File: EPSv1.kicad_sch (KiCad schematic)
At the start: 0 parts

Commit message: first commit
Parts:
- added BT1, BT2: Battery_Cell, symbol Device:Battery_Cell
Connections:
- net BQ29700_1/CELL+: now also BT1.1 (+)
- net BQ29700_1/CELL-: now also BT1.2 (-)
- net BQ29700_2/CELL+: now also BT2.1 (+)
- net BQ29700_2/CELL-: now also BT2.2 (-)
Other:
- sheet Untitled Sheet renamed MCP73831_1
- added sheet MCP73831_2 (../PCB_Schematic_Blocks_Library/MCP73831.kicad_sch)
- sheet MCP73831_1 ports: added GND; removed none

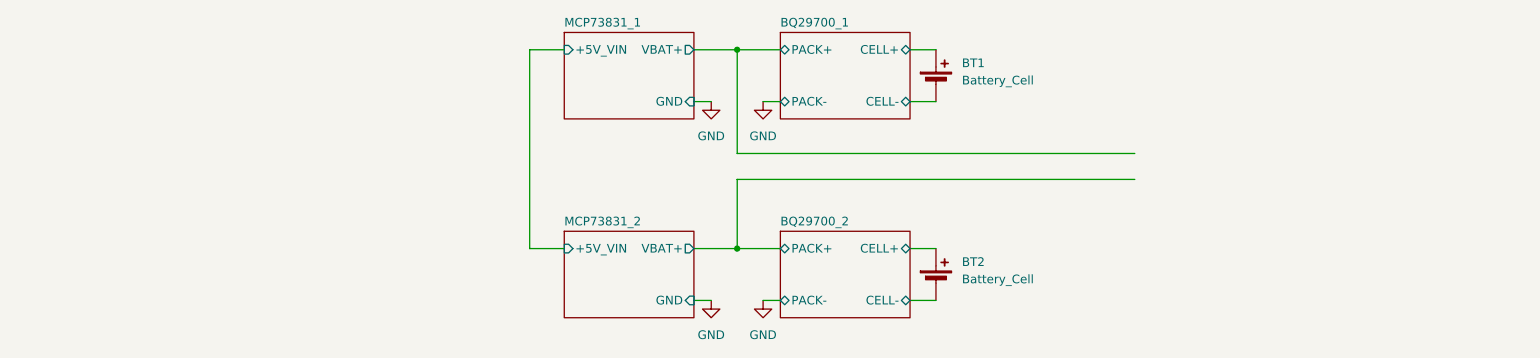
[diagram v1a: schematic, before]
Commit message: added molex nanofit
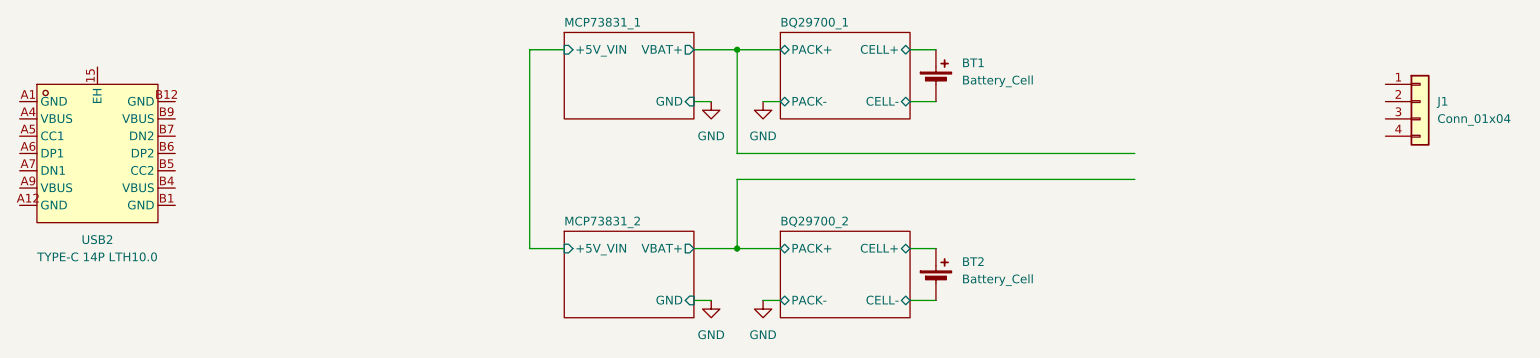
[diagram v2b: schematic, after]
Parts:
- added J1: Conn_01x04, Rocketry_Manual:1054301102, symbol Connector_Generic:Conn_01x04
- added USB2: TYPE-C 14P LTH10.0, Rocketry_Easyeda:TYPE-C-SMD_918-468K2029Y50001, symbol Rocketry_Easyeda:TYPE-C14PLTH10.0
- BT1, BT2: footprint (none) -> Rocketry_Manual:BAT_1121
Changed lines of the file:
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@@
 			)
 		)
-		(property "Footprint" ""
+		(property "Footprint" "Rocketry_Manual:BAT_1121"
 			(at 156.21 94.996 90)
 			(effects
@@
 				(path "/61d36b12-c329-4dd2-b08b-b63678fc7b25"
 					(reference "BT2")
+					(unit 1)
+				)
+			)
+		)
+	)
+	(symbol
+		(lib_id "Rocketry_Easyeda:TYPE-C14PLTH10.0")
+		(at 33.02 76.2 0)
+		(unit 1)
+		(exclude_from_sim no)
+		(in_bom yes)
+		(on_board yes)
+		(dnp no)
+		(fields_autoplaced yes)
+		(property "Reference" "USB2"
+			(at 33.02 90.17 0)
+			(effects
+				(font
+					(size 1.27 1.27)
+				)
+			)
+		)
+		(property "Value" "TYPE-C 14P LTH10.0"
+			(at 33.02 92.71 0)
+			(effects
+				(font
+					(size 1.27 1.27)
+				)
+			)
+		)
+		(property "Footprint" "Rocketry_Easyeda:TYPE-C-SMD_918-468K2029Y50001"
+			(at 33.02 92.71 0)
+			(effects
+				(font
+					(size 1.27 1.27)
+				)
+				(hide yes)
+			)
+		)
+		(property "Datasheet" ""
+			(at 33.02 76.2 0)
+			(effects
+				(font
+					(size 1.27 1.27)
+				)
+				(hide yes)
+			)
+		)
+		(property "Description" ""
+			(at 33.02 76.2 0)
+			(effects
+				(font
+					(size 1.27 1.27)
+				)
+				(hide yes)
+			)
+		)
+		(property "LCSC Part" "C5187467"
+			(at 33.02 95.25 0)
+			(effects
+				(font
+					(size 1.27 1.27)
+				)
+				(hide yes)
+			)
+		)
+		(pin "B9"
+		)
+		(pin "B4"
+		)
+		(pin "A9"
+		)
+		(pin "B7"
+		)
+		(pin "A4"
+		)
+		(pin "A12"
+		)
+		(pin "A1"
+		)
+		(pin "B5"
+		)
+		(pin "B12"
+		)
+		(pin "15"
+		)
+		(pin "A5"
+		)
+		(pin "A6"
+		)
+		(pin "B6"
+		)
+		(pin "A7"
+		)
+		(pin "B1"
+		)
+		(instances
+			(project ""
+				(path "/61d36b12-c329-4dd2-b08b-b63678fc7b25"
+					(reference "USB2")
+					(unit 1)
+				)
+			)
+		)
+	)
+	(symbol
+		(lib_id "Connector_Generic:Conn_01x04")
+		(at 227.33 69.85 0)
+		(unit 1)
+		(exclude_from_sim no)
+		(in_bom yes)
+		(on_board yes)
+		(dnp no)
+		(fields_autoplaced yes)
+		(property "Reference" "J1"
+			(at 229.87 69.8499 0)
+			(effects
+				(font
+					(size 1.27 1.27)
+				)
+				(justify left)
+			)
+		)
+		(property "Value" "Conn_01x04"
+			(at 229.87 72.3899 0)
+			(effects
+				(font
+					(size 1.27 1.27)
+				)
+				(justify left)
+			)
+		)
+		(property "Footprint" "Rocketry_Manual:1054301102"
+			(at 227.33 69.85 0)
+			(effects
+				(font
+					(size 1.27 1.27)
+				)
+				(hide yes)
+			)
+		)
+		(property "Datasheet" "~"
+			(at 227.33 69.85 0)
+			(effects
+				(font
+					(size 1.27 1.27)
+				)
+				(hide yes)
+			)
+		)
+		(property "Description" "Generic connector, single row, 01x04, script generated (kicad-library-utils/schlib/autogen/connector/)"
+			(at 227.33 69.85 0)
+			(effects
+				(font
+					(size 1.27 1.27)
+				)
+				(hide yes)
+			)
+		)
+		(pin "2"
+		)
+		(pin "3"
+		)
+		(pin "4"
+		)
+		(pin "1"
+		)
+		(instances
+			(project ""
+				(path "/61d36b12-c329-4dd2-b08b-b63678fc7b25"
+					(reference "J1")
 					(unit 1)
 				)
@@
 		(dnp no)
 		(fields_autoplaced yes)
-		(property "Reference" "#PWR01"
+		(property "Reference" "#PWR02"
 			(at 123.19 105.41 0)
 			(effects
@@
 			(project ""
 				(path "/61d36b12-c329-4dd2-b08b-b63678fc7b25"
-					(reference "#PWR01")
+					(reference "#PWR02")
 					(unit 1)
 				)
@@
 			)
 		)
-		(property "Footprint" ""
+		(property "Footprint" "Rocketry_Manual:BAT_1121"
 			(at 156.21 65.786 90)
 			(effects
@@
 		(dnp no)
 		(fields_autoplaced yes)
-		(property "Reference" "#PWR02"
+		(property "Reference" "#PWR01"
 			(at 123.19 76.2 0)
 			(effects
@@
 			(project "EPSv1"
 				(path "/61d36b12-c329-4dd2-b08b-b63678fc7b25"
-					(reference "#PWR02")
-					(unit 1)
-				)
+					(reference "#PWR01")
+					(unit 1)
+				)

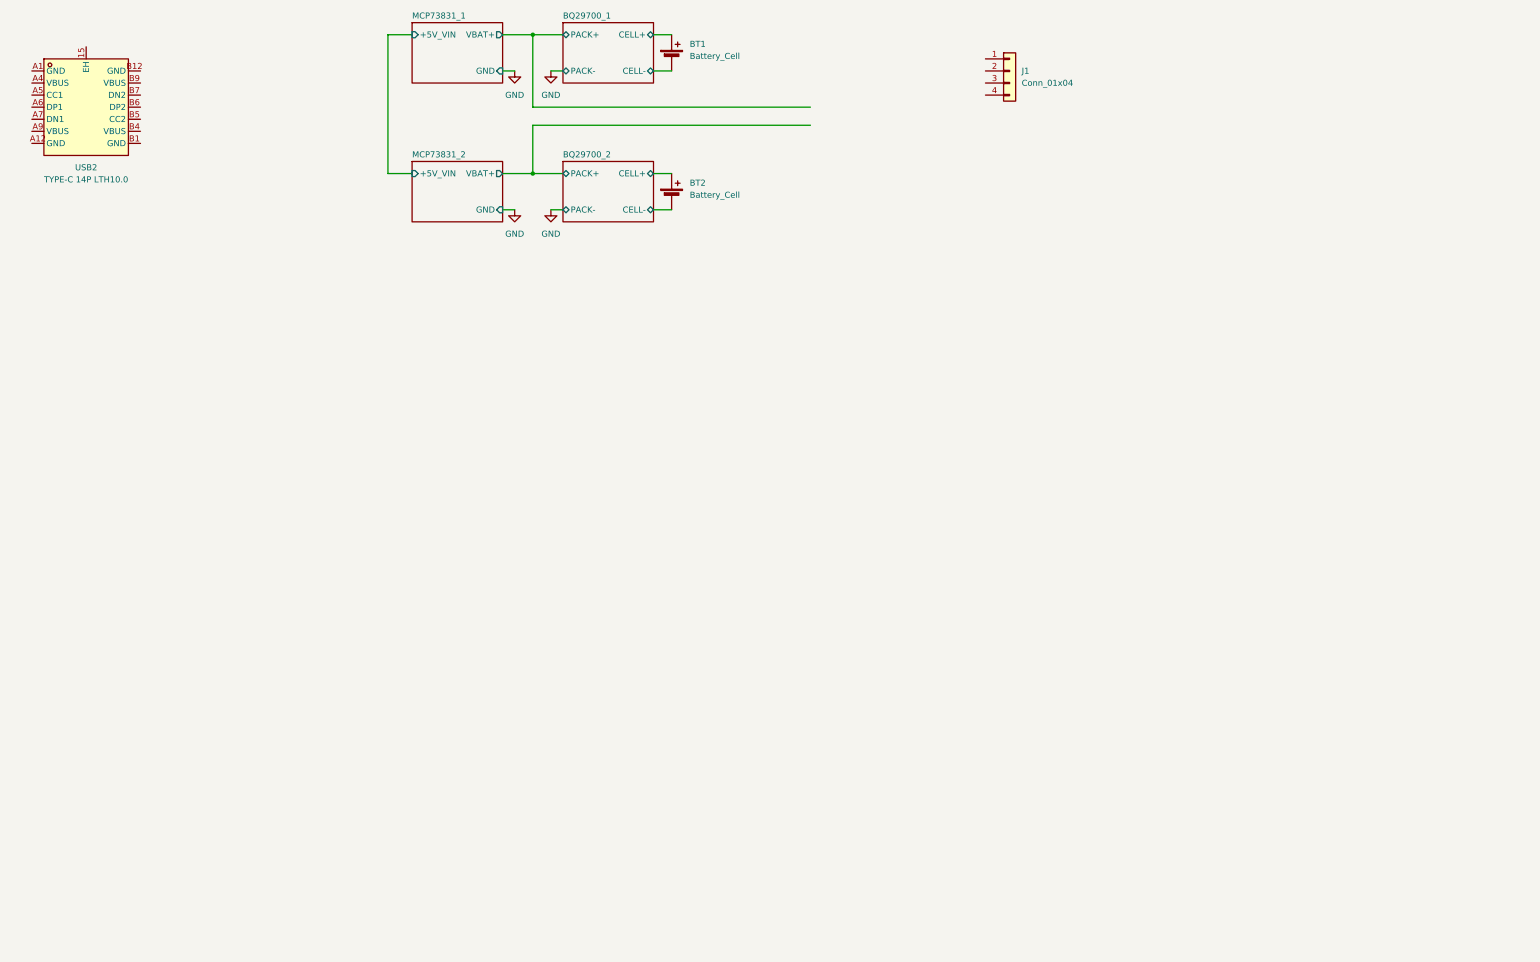
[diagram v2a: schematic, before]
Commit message: Laid out all the blocks and imported the board outline
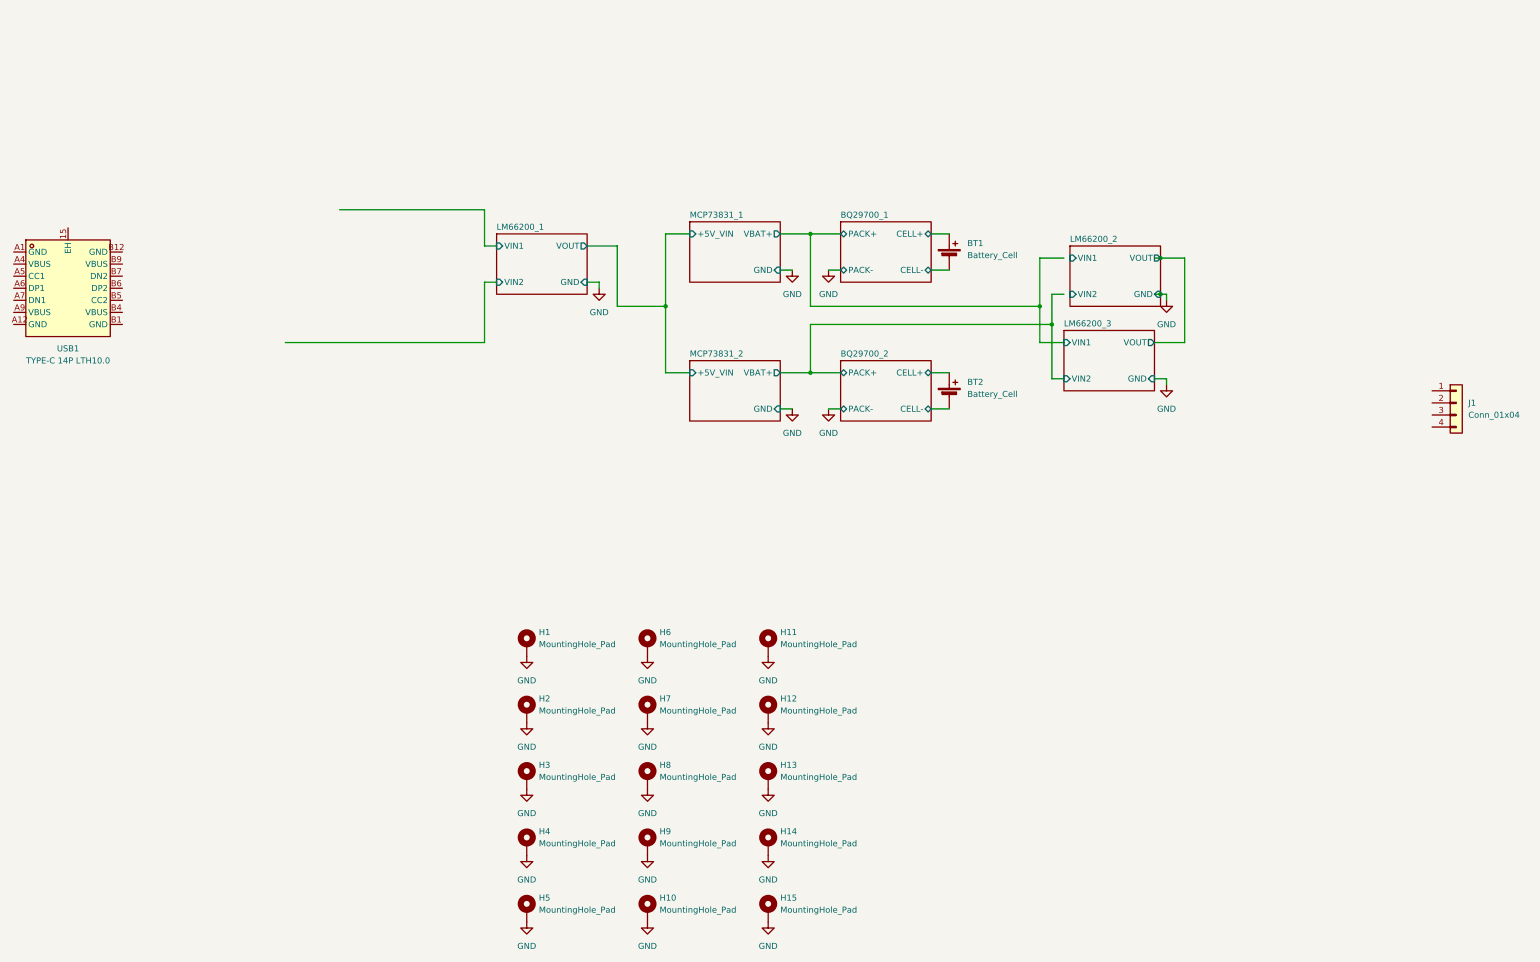
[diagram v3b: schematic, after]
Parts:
- added H1, H10, H11, H12, H13, H14, H15, H2, H3, H4, H5, H6, H7, H8, H9: MountingHole_Pad, MountingHole:MountingHole_2.7mm_M2.5_Pad_Via, symbol Mechanical:MountingHole_Pad
- renumbered USB2 to USB1
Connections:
- net GND: now also H1.1, H10.1, H11.1, H12.1, H13.1, H14.1, H15.1, H2.1, H3.1, H4.1, H5.1, H6.1, H7.1, H8.1, H9.1
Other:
- added sheet LM66200_1 (../PCB_Schematic_Blocks_Library/LM66200.kicad_sch)
- added sheet LM66200_2 (../PCB_Schematic_Blocks_Library/LM66200.kicad_sch)
- added sheet LM66200_3 (../PCB_Schematic_Blocks_Library/LM66200.kicad_sch)
- moved on the sheet: BT1, BT2, J1, USB1

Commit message: 100x100 board size
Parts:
- removed H10, H11, H12, H13, H14, H15, H5, H6, H7, H8, H9: MountingHole_Pad, MountingHole:MountingHole_2.7mm_M2.5_Pad_Via, symbol Mechanical:MountingHole_Pad
- added J3, J4: Molex_Microfit, Rocketry_Manual:1054301102, symbol Connector_Generic:Conn_01x04
- added U10: MCP9700AT-E/TT, Rocketry_Easyeda:SOT-23-3_L2.9-W1.3-P1.90-LS2.4-BR, symbol Rocketry_Easyeda:MCP9700AT-E_TT
- J1: value Conn_01x04 -> Molex_Microfit
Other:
- added sheet LM66200_4 (../PCB_Schematic_Blocks_Library/LM66200.kicad_sch)
- added sheet LM66200_5 (../PCB_Schematic_Blocks_Library/LM66200.kicad_sch)
- added sheet LM66200_6 (../PCB_Schematic_Blocks_Library/LM66200.kicad_sch)
- added sheet STM32L432KCUx (../PCB_Schematic_Blocks_Library/STM32L432KCUx.kicad_sch)
- sheet LM66200_1 ports: added ~{ON}; removed none
- sheet LM66200_2 ports: added ~{ON}; removed none
- sheet LM66200_3 ports: added ~{ON}; removed none
- moved on the sheet: BT1, BT2, H1, H2, H3, J1, USB1

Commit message: adde new blocks
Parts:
- added R1, R2, R3, R4: 470k 0603, Rocketry_Easyeda:R0603, symbol Rocketry_Easyeda:0603WAF4703T5E (470k 0603)
- added U1: MCP9700AT-E/TT, Rocketry_Easyeda:SOT-23-3_L2.9-W1.3-P1.90-LS2.4-BR, symbol Rocketry_Easyeda:MCP9700AT-E_TT
- renumbered J4 to J1, J3 to J2, J1 to J3, U10 to U2
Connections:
- net GND: now also U2.3 (GND), R2.1, R4.1, U1.3 (GND)
- net +5V: now reaches U2.1 (VDD)
- net +5V: now also U1.1 (VDD)
- net PB1: now reaches U2.2 (VOUT)
- net BQ29700_1/CELL+ renamed CELL_1+
- net CELL_1+: now also R1.2
- net BQ29700_2/CELL+ renamed CELL_2+
- net CELL_2+: now also R3.2
- new net PA0: R1.1, R2.2
- new net PA1: R3.1, R4.2
- new net PB0: U1.2 (VOUT)
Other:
- added sheet Reverse_Polarity (../PCB_Schematic_Blocks_Library/Reverse_Polarity_Block.kicad_sch)
- added sheet TPS63070_3.3V (../PCB_Schematic_Blocks_Library/TPS63070_3.3V.kicad_sch)
- moved on the sheet: H1, H2, H3, H4, U2

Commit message: exported STEP
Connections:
- net +3.3V: now also U1.1 (VDD), U2.1 (VDD)
- net +5V: no longer U1.1 (VDD), U2.1 (VDD)
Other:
- added sheet TPS63070_5V (../PCB_Schematic_Blocks_Library/TPS63070_5V.kicad_sch)
- moved on the sheet: BT1, BT2, U1, U2, USB1

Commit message: started proper layout
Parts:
- removed BT1, BT2: Battery_Cell, Rocketry_Manual:BAT_1121, symbol Device:Battery_Cell
- removed J1, J2, J3: Molex_Microfit, Rocketry_Manual:1054301102, symbol Connector_Generic:Conn_01x04
- removed USB1: TYPE-C 14P LTH10.0, Rocketry_Easyeda:TYPE-C-SMD_918-468K2029Y50001, symbol Rocketry_Easyeda:TYPE-C14PLTH10.0
- added BT1: 2P 21700 Cell Holder, Rocketry_Manual:PA21700x2-THM_Parallel, symbol Connector_Generic:Conn_02x02_Counter_Clockwise
- added J1, J3, J4: 1053091102, Rocketry_Manual:CON_1053091102, symbol Rocketry_Manual:1053091102
- added R36, R37, R38: 100k 0603, Rocketry_Easyeda:R0603, symbol Rocketry_Easyeda:0603WAF1003T5E (100k 0603)
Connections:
- net CELL_1+: now also BT1.4 (Pin_4)
- net CELL_2+: now also BT1.1 (Pin_1)
- net GND: now also J1.2, J3.2, J4.2, R36.1, R37.1, R38.1
- net LM66200_4/VOUT: now also J1.1
- net LM66200_5/VOUT: now also J3.1
- net LM66200_6/VOUT: now also J4.1
- net ~{MCU_LS_1}: now also R36.2
- net ~{MCU_LS_2}: now also R37.2
- net ~{MCU_LS_3}: now also R38.2
- new net CELL_1-: BT1.3 (Pin_3)
- new net CELL_2-: BT1.2 (Pin_2)
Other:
- sheet STM32L432KCUx ports: added USB_+5V; removed none
- note added: "100k pulldowns to keep the default state ON"

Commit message: v0.1 sent to JLCPCB
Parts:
- added C37, C38, C39, C40, C41, C42, C43, C44, C45, C46: 10uF 0603, Rocketry_Easyeda:C0603, symbol Rocketry_Easyeda:CL10A106KP8NNNC (10uF 0603)
- added TP1, TP10, TP2, TP3, TP4, TP5, TP6, TP7, TP8, TP9: TestPoint, TestPoint:TestPoint_Pad_1.0x1.0mm, symbol Connector:TestPoint
- added U26: 1.5uF 2.9A, Rocketry_Easyeda:IND-SMD_L2.5-W2.0_MEKK2520TR47M, symbol Rocketry_Easyeda:FTC252012S1R5MBCA (1.5uF 2.9A)
- renumbered J3 to J2, J4 to J3, R36 to R5, R37 to R6, R38 to R7
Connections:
- net +3.3V: now also C37.2, C38.2, C39.2, C40.2, C41.2, TP6.1, U26.1
- net +5V: now also TP5.1
- net CELL_1+: now also TP1.1
- net CELL_2+: now also TP2.1
- net GND: now also C37.1, C38.1, C39.1, C40.1, C41.1, C42.1, C43.1, C44.1, C45.1, C46.1, TP10.1, TP8.1, TP9.1
- net PB0: now also TP3.1
- net PB1: now also TP4.1
- net STM32L432KCUx/+3V3A: now also C42.2, C43.2, C44.2, C45.2, C46.2, U26.2
- net LM66200_4/VOUT renamed INA199_1/IN-
- net LM66200_5/VOUT renamed INA199_2/IN-
- net LM66200_6/VOUT renamed INA199_3/IN-
- new net +9V: TP7.1
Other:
- added sheet INA199_1 (INA199.kicad_sch)
- added sheet INA199_2 (INA199.kicad_sch)
- added sheet INA199_3 (INA199.kicad_sch)
- added sheet TPS63070_9V (TPS63070_9V.kicad_sch)
- sheet STM32L432KCUx: file ../PCB_Schematic_Blocks_Library/STM32L432KCUx.kicad_sch -> D:/documents/KiCadProjects/EPSv1/STM32L432KCUx.kicad_sch
- sheet STM32L432KCUx ports: added GND; removed none
- moved on the sheet: BT1, J1, J2, J3, R5, R6, R7
